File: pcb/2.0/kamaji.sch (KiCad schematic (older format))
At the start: 42 parts, among them J1 RJ10, J2 RJ10, J3 RJ10, J4 RJ10, J5 RJ10, J6 Daughter board, J7 ICSP, J8 USB_B, J9 USB_A, Q2 IRL540N, Q3 IRL540N, SW1 SW_Push, SW2 SW_Push, SW3 SW_Push, U1 ATMEGA32U4-AU, Y1 16MHz

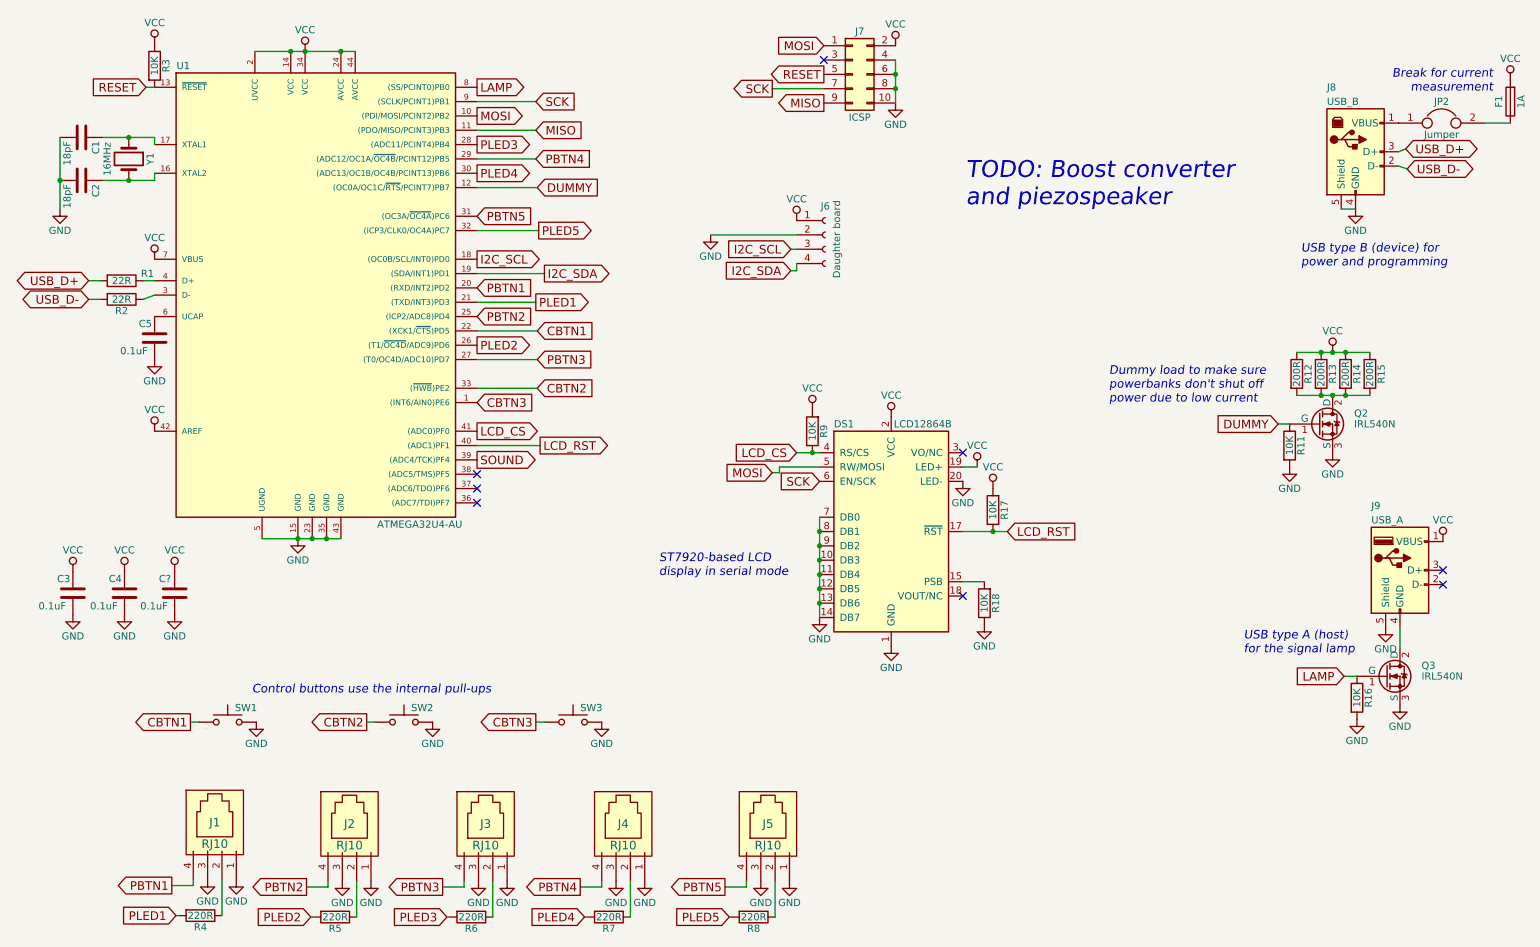
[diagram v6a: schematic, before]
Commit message: add boost converter, move LCD to a separate sheet
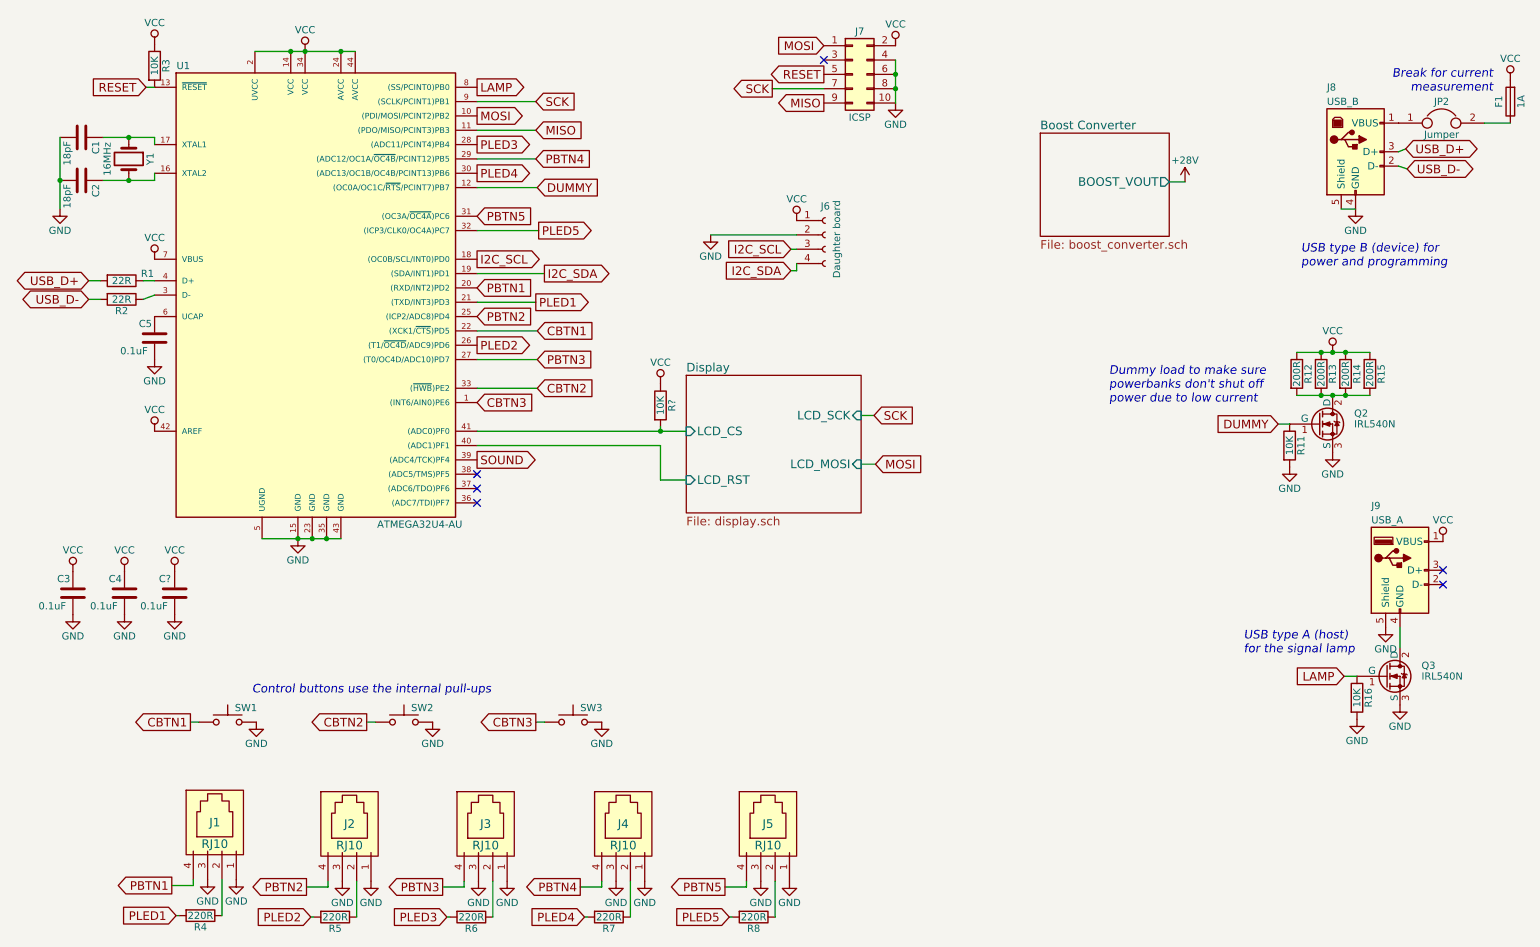
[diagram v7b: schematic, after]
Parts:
- removed DS1: LCD12864B, kamaji:LCD12864B, symbol LCD12864B
- removed R17, R18, R9: 10K, symbol R
- added R?: 10K, symbol R
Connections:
- net VCC: now also R?.1
- net LCD_CS renamed Display/LCD_CS
- net Display/LCD_CS: now also R?.2
- net LCD_RST renamed Display/LCD_RST
- no-connect marks 8 -> 6
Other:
- note removed: "ST7920-based LCD\ndisplay in serial mode"
- note removed: "TODO: Boost converter\nand piezospeaker"

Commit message: use a 6-pin ICSP connector
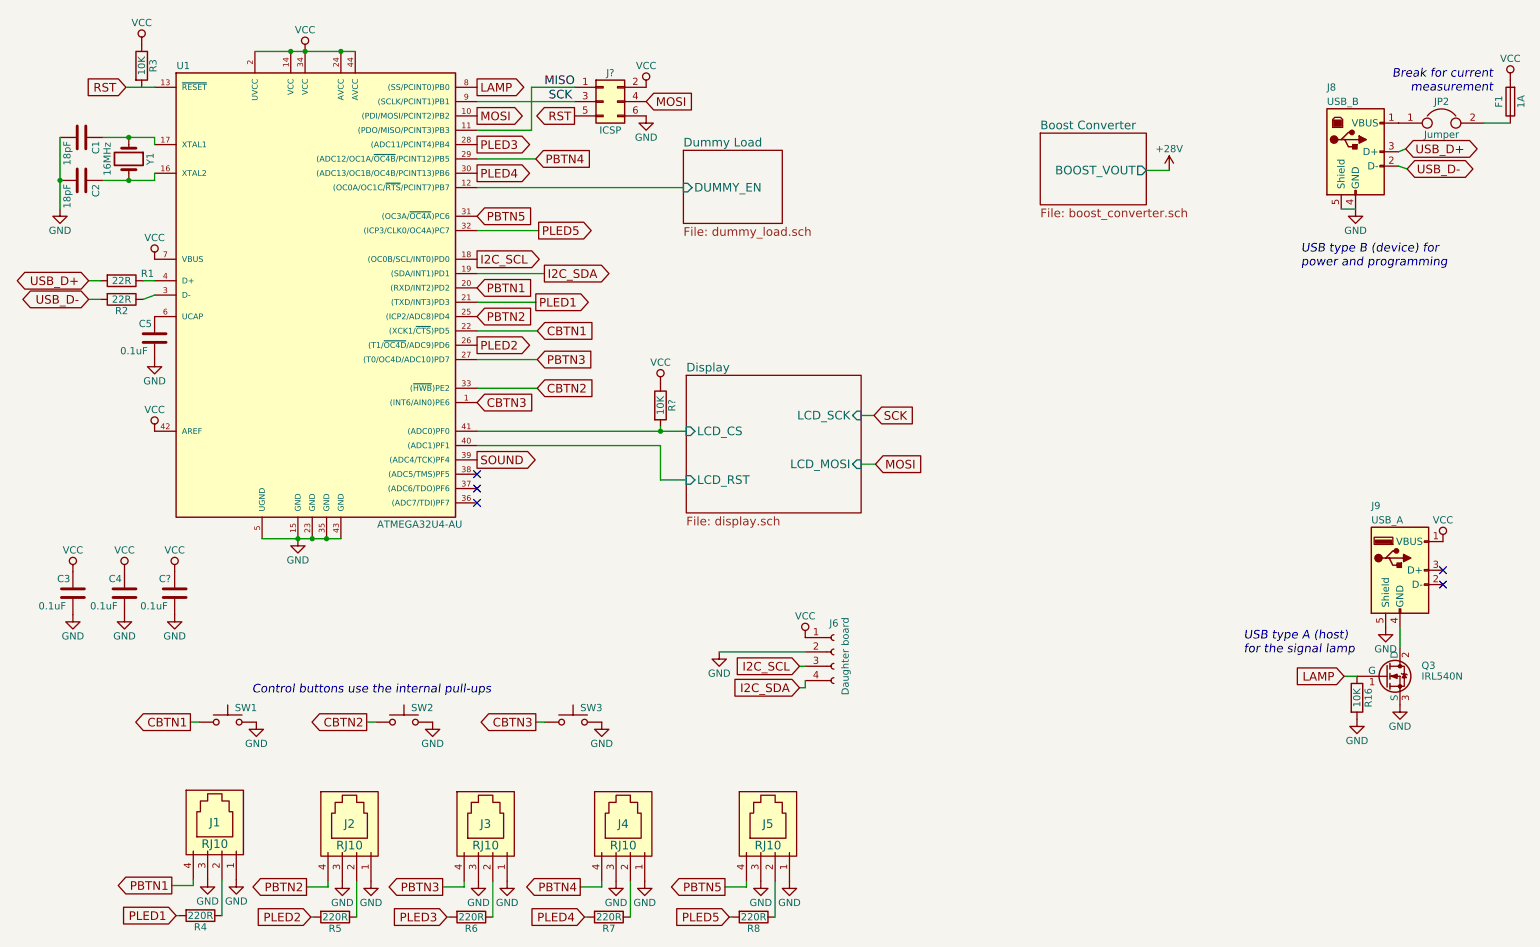
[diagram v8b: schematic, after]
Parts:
- removed J7: ICSP, symbol Conn_02x05_Odd_Even
- removed Q2: IRL540N, TO_SOT_Packages_THT:TO-220-3_Horizontal, symbol IRLIZ44N
- removed R11: 10K, symbol R
- removed R12, R13, R14, R15: 200R, symbol R
- added J?: ICSP, symbol Conn_02x03_Odd_Even
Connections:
- net GND: now also J?.6 (Pin_6)
- net MISO: now also J?.1 (Pin_1)
- net MOSI: now also J?.4 (Pin_4)
- net SCK: now also J?.3 (Pin_3)
- net VCC: now also J?.2 (Pin_2)
- net DUMMY renamed Dummy Load/DUMMY_EN
- net RESET: no longer names the net of R3.2
- net RESET: no longer U1.13 (~RESET~)
- new net RST: J?.5 (Pin_5), U1.13 (~RESET~)
- no-connect marks 6 -> 5
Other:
- note removed: "Dummy load to make sure\npowerbanks don't shut off\npower due to low current"
- moved on the sheet: J6, R3
